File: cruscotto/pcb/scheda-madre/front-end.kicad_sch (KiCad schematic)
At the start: 46 parts, among them J3 USB-C (solo a banco), J4 Ventola 4 fili, J5 NTC display, Q3 ZXMP6A13F (P 60 V), Q4 MMBTA06 (80 V), Q5 MMBT3904, Q6 MMBT3904, Q7 MMBT3904, SW3 RESET, SW4 BOOT, U4 ESP32-WROOM-32E-H4, U5 AP2112K-3.3, U6 CH340C

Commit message: docs: D-052 dashboard fan Delta AFB0412VA-00; J4 value and wire colours in CR-EL-002
Co-Authored-By: Claude Opus 5.5 <noreply@anthropic.com>
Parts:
- J4: value Ventola 4 fili -> Ventola Delta AFB0412VA-00 (D-052)
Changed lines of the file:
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@@
 	(symbol (lib_id "Connector_Generic:Conn_01x04") (at 325.12 187.96 0) (unit 1) (exclude_from_sim no) (in_bom yes) (on_board yes) (dnp no)
 		(property "Reference" "J4" (at 325.12 179.07 0) (effects (font (size 1.27 1.27))))
-		(property "Value" "Ventola 4 fili" (at 325.12 181.61 0) (effects (font (size 1.27 1.27))))
+		(property "Value" "Ventola Delta AFB0412VA-00 (D-052)" (at 325.12 181.61 0) (effects (font (size 1.27 1.27))))
 		(property "Footprint" "Connector:FanPinHeader_1x04_P2.54mm_Vertical" (at 325.12 187.96 0) (hide yes) (effects (font (size 1.27 1.27))))
 		(property "Datasheet" "" (at 325.12 187.96 0) (hide yes) (effects (font (size 1.27 1.27))))
-		(property "Description" "" (at 325.12 187.96 0) (hide yes) (effects (font (size 1.27 1.27))))
+		(property "Description" "Fili Delta: nero GND, rosso +12V, blu giri, giallo PWM" (at 325.12 187.96 0) (hide yes) (effects (font (size 1.27 1.27))))
 		(pin "1")
 		(pin "2")

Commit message: feat(schematic): D-054 dashboard buttons, S1 to S3 IO19 and S2 to front-end GPIO5
S1/S2 symbols match the PCB switches; GPIO5 pull-up 10k; GPIO table and S3 connector table updated. 97 nets checked, ERC 0 errors.

Co-Authored-By: Claude Opus 5.5 <noreply@anthropic.com>
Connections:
- net FE_BTN2: now reaches U4.29 (IO5)
- no-connect marks 20 -> 19
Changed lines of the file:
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@@
 	(no_connect (at 190.5 119.38))
 	(no_connect (at 218.44 109.22))
-	(no_connect (at 218.44 99.06))
 	(no_connect (at 190.5 144.78))
 	(wire (pts (xy 187.96 91.44) (xy 185.42 91.44)) (stroke (width 0) (type default)))
@@
 	(global_label "KL_TX" (shape passive) (at 220.98 114.3 0) (fields_autoplaced yes) (effects (font (size 1.27 1.27)) (justify left))
 		(property "Intersheetrefs" "${INTERSHEET_REFS}" (at 220.98 114.3 0) (effects (font (size 1.27 1.27)) (justify left) (hide yes))))
+	(wire (pts (xy 218.44 99.06) (xy 220.98 99.06)) (stroke (width 0) (type default)))
+	(global_label "FE_BTN2" (shape passive) (at 220.98 99.06 0) (fields_autoplaced yes) (effects (font (size 1.27 1.27)) (justify left))
+		(property "Intersheetrefs" "${INTERSHEET_REFS}" (at 220.98 99.06 0) (effects (font (size 1.27 1.27)) (justify left) (hide yes))))
 	(wire (pts (xy 218.44 116.84) (xy 220.98 116.84)) (stroke (width 0) (type default)))
 	(global_label "SD_SCK" (shape passive) (at 220.98 116.84 0) (fields_autoplaced yes) (effects (font (size 1.27 1.27)) (justify left))

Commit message: feat(pcb): D-059 wires soldered to the mainboard, re-routed; BOM with Farnell availability
- D-059: fan (J4), display NTC (J5) and S3 cables (J10-J12) on 26 AWG solder-wire pads instead of
  connectors; MicroSD, VAN and IMU modules soldered directly. Schematic sheets EL-002 rev B,
  EL-004 rev C, EL-005 rev B (27/10/2026); J11 moved 2.5 mm outward for J1 clearance.
- Placement and routing redone: 3987 tracks, 514 vias; DRC 0 errors, 0 unconnected, no hole or
  dangling warnings; 92 silkscreen warnings left.
- completa-sbroglio-scheda-madre.py: drill map so new vias keep the 0.25 mm hole-to-hole distance
  from every drill, including same-net ones.
- BOM: everything needed except consumables; parts shared with the Data Logger order flagged
  (LM2903B spare, EEEHB1C100R; second VAN and SD modules needed).
- tools/controlla-distinta-farnell.py (element14 Product Search API, key read from env or
  ~/.farnell_api_key, never printed) and the 27/10/2026 Farnell snapshot: 10 items not stocked
  (ESP32-WROOM-32E-H4, TPS54360B, LMR36510, LM74700-Q1, CH340C, AO3400A, SRR1260-8R2Y, HRO USB-C,
  7.3 mm tactile switches, AFB0412VA-00), 4 at zero stock.

Limits: routing checked only by DRC; nothing ordered, built or tested.

Co-Authored-By: Claude Opus 5.5 <noreply@anthropic.com>
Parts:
- J4: footprint Connector:FanPinHeader_1x04_P2.54mm_Vertical -> Connector_Wire:SolderWire-0.127sqmm_1x04_P3.7mm_D0.48mm_OD1mm
- J5: footprint Connector_JST:JST_XH_B2B-XH-A_1x02_P2.50mm_Vertical -> Connector_Wire:SolderWire-0.127sqmm_1x02_P3.7mm_D0.48mm_OD1mm
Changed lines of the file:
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@@
 	(title_block
 		(title "Scheda madre cruscotto C3+AI - front-end ESP32")
-		(date "2026-10-24")
-		(rev "A")
+		(date "2026-10-27")
+		(rev "B")
 		(company "Cruscotto C3+AI")
-		(comment 1 "C3AI-CR-EL-002 rev A - proposta preliminare, non verificata")
-		(comment 2 "D-029, D-031, D-033, D-039, D-046")
+		(comment 1 "C3AI-CR-EL-002 rev B - proposta preliminare, non verificata")
+		(comment 2 "D-029, D-031, D-033, D-039, D-046, D-059")
 		(comment 3 "Generato da tools/genera-schema-scheda-madre.py")
 	)
@@
 		(property "Reference" "J5" (at 345.44 153.67 0) (effects (font (size 1.27 1.27)) (justify left)))
 		(property "Value" "NTC display" (at 345.44 156.21 0) (effects (font (size 1.27 1.27)) (justify left)))
-		(property "Footprint" "Connector_JST:JST_XH_B2B-XH-A_1x02_P2.50mm_Vertical" (at 342.9 154.94 0) (hide yes) (effects (font (size 1.27 1.27))))
+		(property "Footprint" "Connector_Wire:SolderWire-0.127sqmm_1x02_P3.7mm_D0.48mm_OD1mm" (at 342.9 154.94 0) (hide yes) (effects (font (size 1.27 1.27))))
 		(property "Datasheet" "" (at 342.9 154.94 0) (hide yes) (effects (font (size 1.27 1.27))))
 		(property "Description" "NTC 100k incollata vicino al display" (at 342.9 154.94 0) (hide yes) (effects (font (size 1.27 1.27))))
@@
 		(property "Reference" "J4" (at 325.12 179.07 0) (effects (font (size 1.27 1.27))))
 		(property "Value" "Ventola Delta AFB0412VA-00 (D-052)" (at 325.12 181.61 0) (effects (font (size 1.27 1.27))))
-		(property "Footprint" "Connector:FanPinHeader_1x04_P2.54mm_Vertical" (at 325.12 187.96 0) (hide yes) (effects (font (size 1.27 1.27))))
+		(property "Footprint" "Connector_Wire:SolderWire-0.127sqmm_1x04_P3.7mm_D0.48mm_OD1mm" (at 325.12 187.96 0) (hide yes) (effects (font (size 1.27 1.27))))
 		(property "Datasheet" "" (at 325.12 187.96 0) (hide yes) (effects (font (size 1.27 1.27))))
 		(property "Description" "Fili Delta: nero GND, rosso +12V, blu giri, giallo PWM" (at 325.12 187.96 0) (hide yes) (effects (font (size 1.27 1.27))))

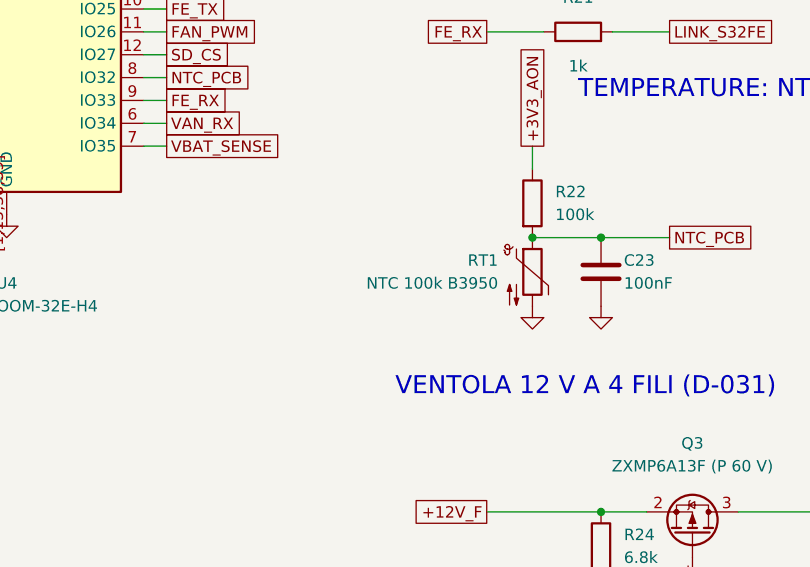
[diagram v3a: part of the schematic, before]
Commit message: feat(bom): S1/S2 Omron B3F-1050, Vishay NTCs with datasheet B value; LCSC cart cross-check
- S1/S2 = Omron B3F-1050 (6x6, 7.3 mm, 100 gf); RT1 = Vishay NTCS0805E3104FXT; display NTC = Vishay
  NTCLE100E3104JB0 (leaded). B value from the datasheets, to be used by the firmware (not B3950).
  Schematic EL-002/EL-005 values and board values updated; footprints unchanged, routing still valid
  (DRC 0 errors, 0 unconnected).
- BOM: LCSC cart of 28/10/2026 (86.37 USD + 13 USD shipping) covers most parts; Q1, L1, C3, R5, R38,
  fan, 22 uF 1206, 10k and 100k from other suppliers; prefer original Diodes AP2112K over the clone.

Co-Authored-By: Claude Opus 5.5 <noreply@anthropic.com>
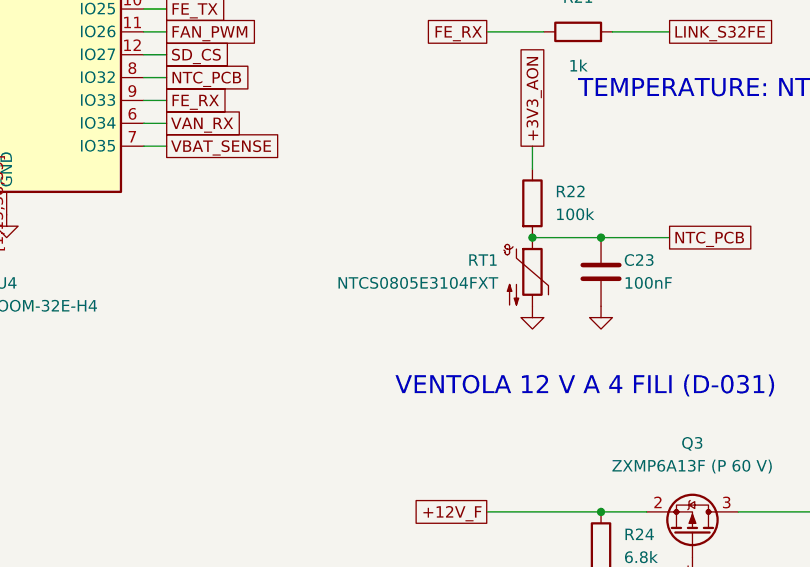
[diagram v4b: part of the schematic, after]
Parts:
- RT1: value NTC 100k B3950 -> NTCS0805E3104FXT
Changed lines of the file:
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@@
 	(symbol (lib_id "Device:Thermistor_NTC") (at 261.62 158.75 0) (unit 1) (exclude_from_sim no) (in_bom yes) (on_board yes) (dnp no)
 		(property "Reference" "RT1" (at 257.81 157.48 0) (effects (font (size 1.27 1.27)) (justify right)))
-		(property "Value" "NTC 100k B3950" (at 257.81 160.02 0) (effects (font (size 1.27 1.27)) (justify right)))
+		(property "Value" "NTCS0805E3104FXT" (at 257.81 160.02 0) (effects (font (size 1.27 1.27)) (justify right)))
 		(property "Footprint" "Resistor_SMD:R_0805_2012Metric_Pad1.20x1.40mm_HandSolder" (at 261.62 158.75 0) (hide yes) (effects (font (size 1.27 1.27))))
 		(property "Datasheet" "" (at 261.62 158.75 0) (hide yes) (effects (font (size 1.27 1.27))))
-		(property "Description" "" (at 261.62 158.75 0) (hide yes) (effects (font (size 1.27 1.27))))
+		(property "Description" "Vishay 100k 1 %; valore B dalla scheda tecnica nel firmware" (at 261.62 158.75 0) (hide yes) (effects (font (size 1.27 1.27))))
 		(pin "1")
 		(pin "2")
@@
 		(property "Footprint" "Connector_Wire:SolderWire-0.127sqmm_1x02_P3.7mm_D0.48mm_OD1mm" (at 342.9 154.94 0) (hide yes) (effects (font (size 1.27 1.27))))
 		(property "Datasheet" "" (at 342.9 154.94 0) (hide yes) (effects (font (size 1.27 1.27))))
-		(property "Description" "NTC 100k incollata vicino al display" (at 342.9 154.94 0) (hide yes) (effects (font (size 1.27 1.27))))
+		(property "Description" "Vishay NTCLE100E3104JB0 (100k) incollata vicino al display; valore B dalla scheda tecnica" (at 342.9 154.94 0) (hide yes) (effects (font (size 1.27 1.27))))
 		(pin "1")
 		(pin "2")
